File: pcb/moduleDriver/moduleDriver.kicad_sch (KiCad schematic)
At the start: 42 parts, among them J1 MOTOR, J10 Sensor, J11 Power, J12 Power, J13 Power, J14 LOOPBACK, J2 MOTOR, J3 MOTOR, J4 MOTOR, J5 IDC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

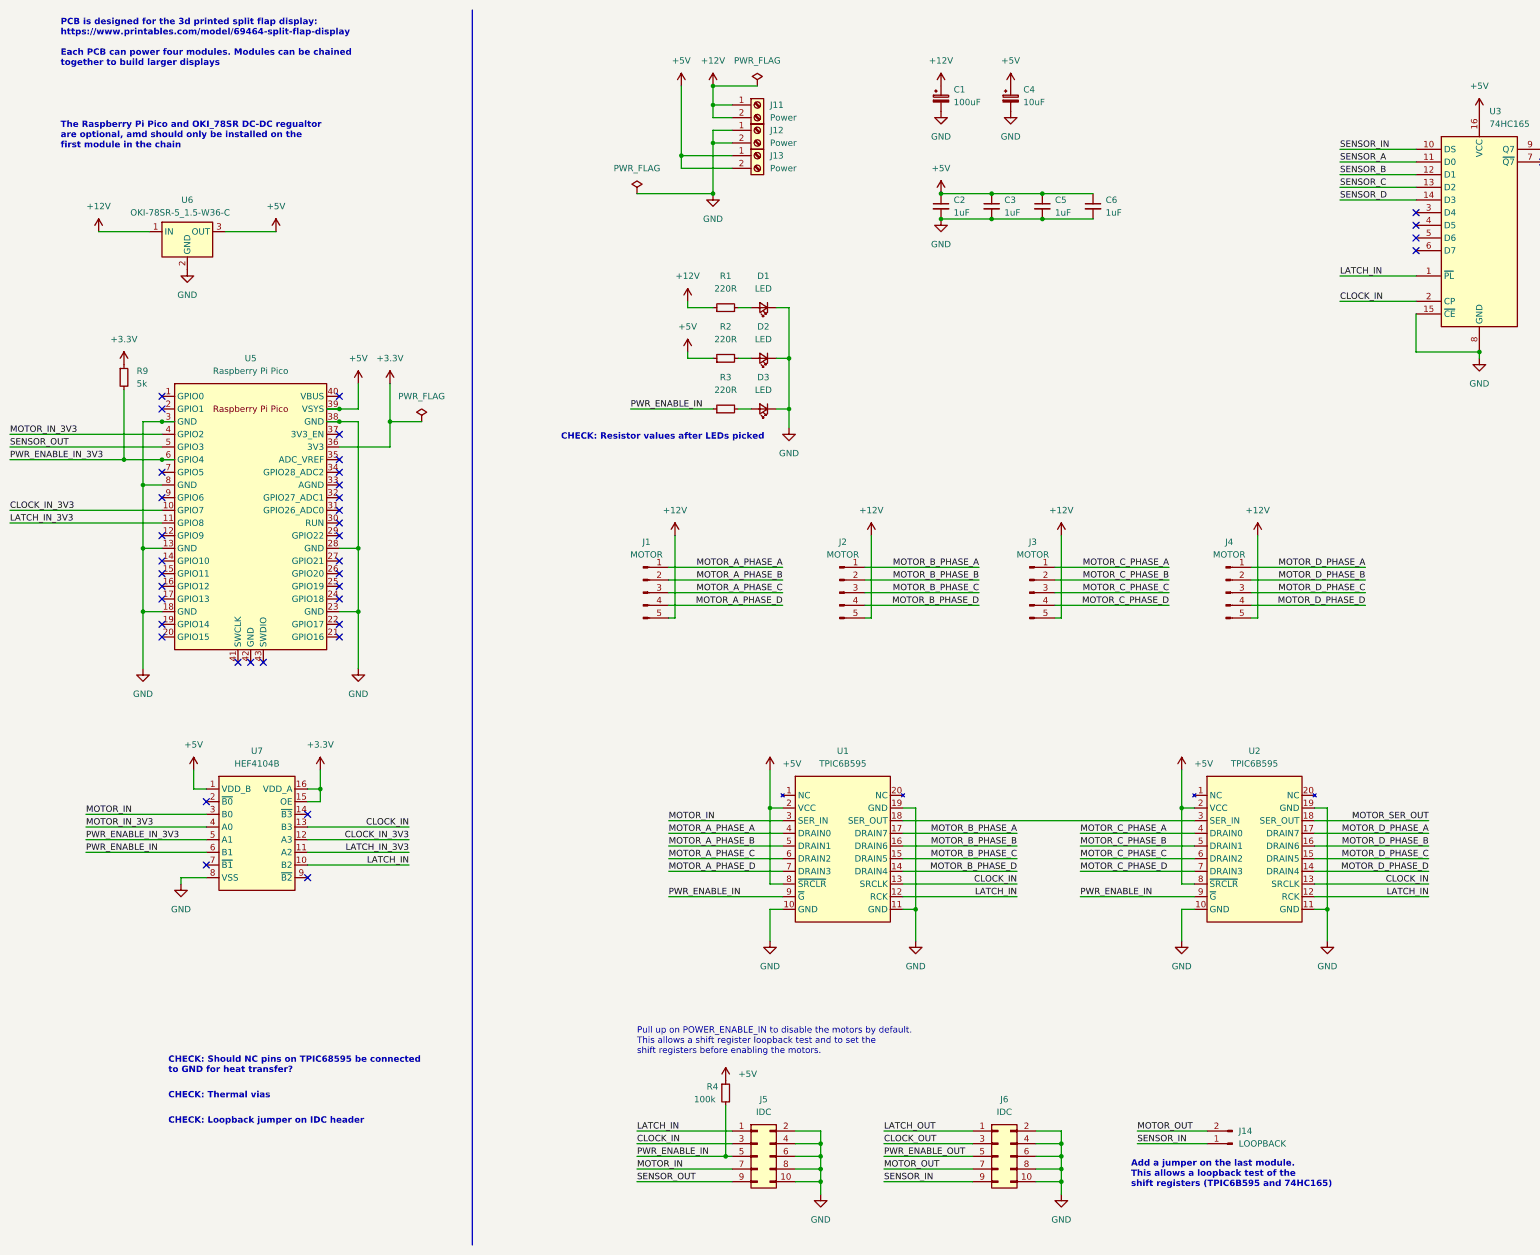
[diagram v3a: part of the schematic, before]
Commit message: Add voltage divider for SENSOR_OUT
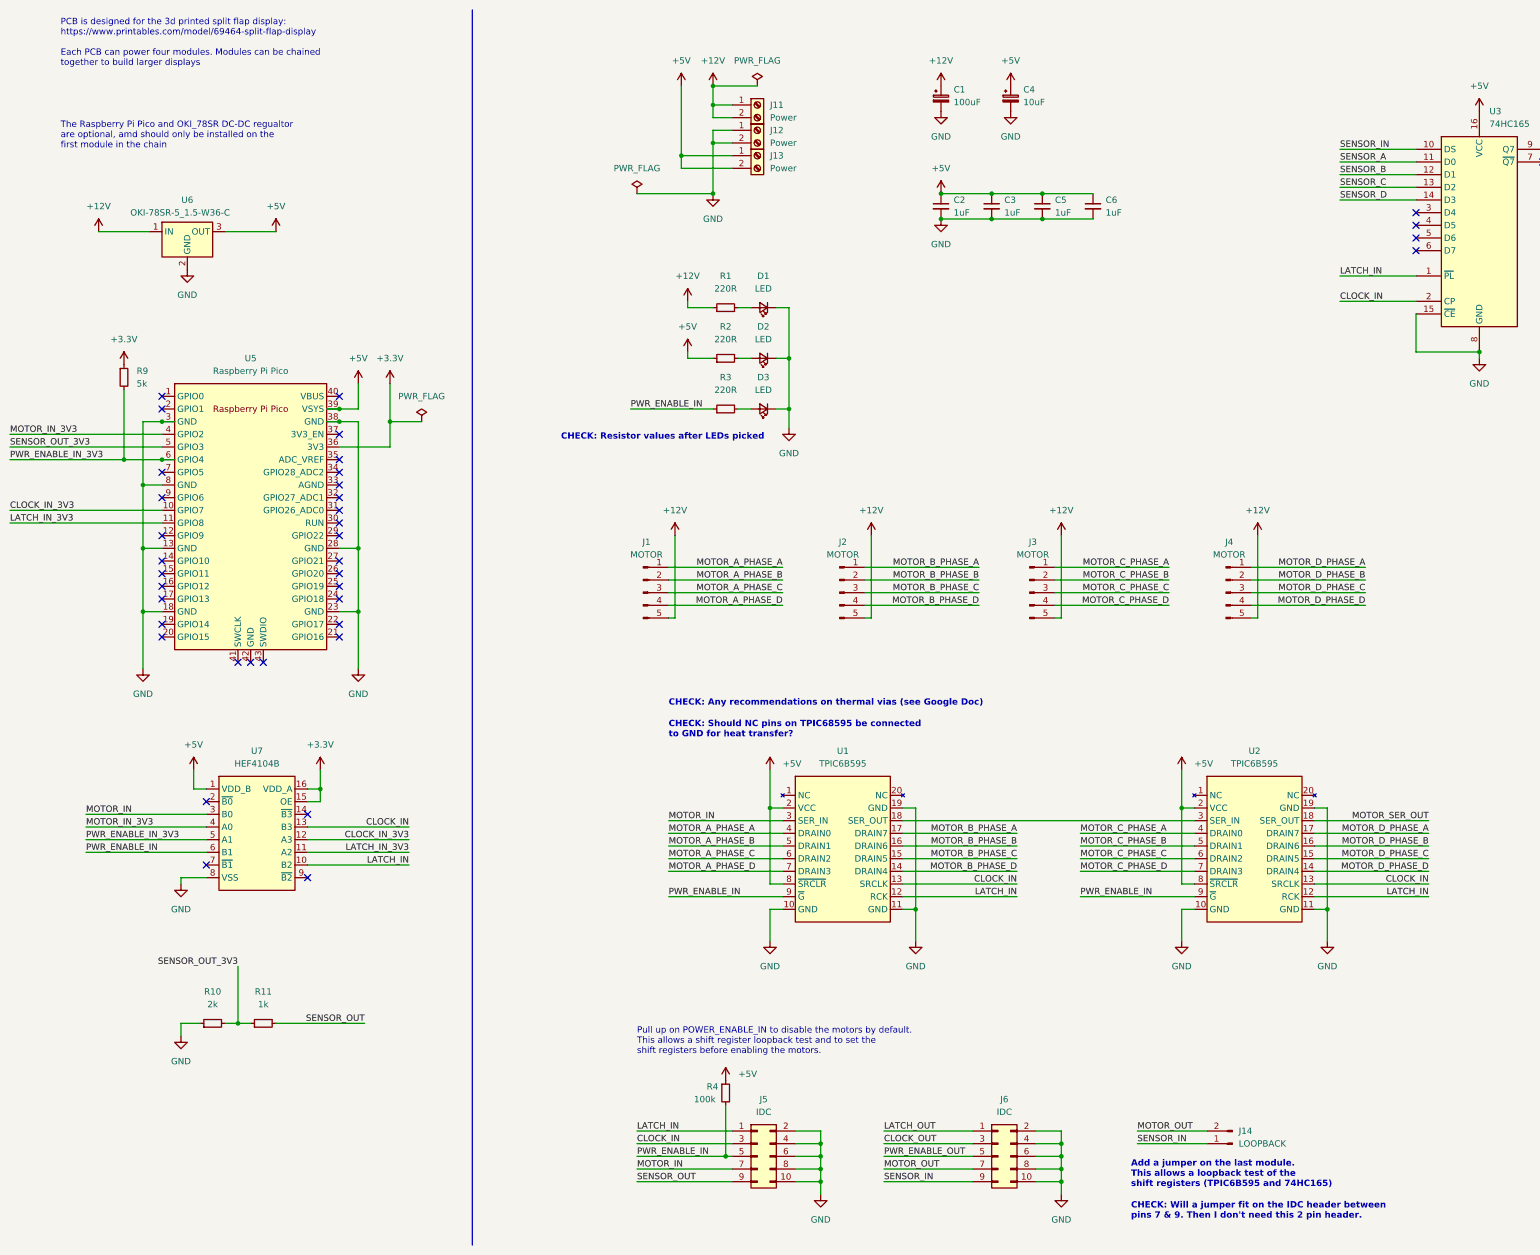
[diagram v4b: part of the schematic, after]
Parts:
- added R10: 2k, Resistor_SMD:R_0603_1608Metric, symbol Device:R_Small
- added R11: 1k, Resistor_SMD:R_0603_1608Metric, symbol Device:R_Small
- U7: footprint (none) -> Package_SO:SOIC-16_4.55x10.3mm_P1.27mm
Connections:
- net GND: now also R10.1
- net SENSOR_OUT: now also R11.2; no longer U5.5 (GPIO3)
- new net SENSOR_OUT_3V3: R10.2, R11.1, U5.5 (GPIO3)
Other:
- note added: "CHECK: Any recommendations on thermal vias (see Google Doc)"
- note added: "CHECK: Will a jumper fit on the IDC header between pins 7 & 9. Then I don't need this 2 pin header."
- note removed: "CHECK: Loopback jumper on IDC header"
- note removed: "CHECK: Thermal vias"
- title: (none) -> Split Flap Module
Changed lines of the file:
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@@
 (kicad_sch (version 20211123) (generator eeschema)
   (paper "A3")
+  (title_block
+    (title "Split Flap Module")
+    (rev "0.2")
+  )
   (junction (at 374.65 64.77) (diameter 0) (color 0 0 0 0)
   )
@@
   )
   (junction (at 41.91 143.51) (diameter 0) (color 0 0 0 0)
+  )
+  (junction (at 60.96 226.06) (diameter 0) (color 0 0 0 0)
   )
   (junction (at 38.1 113.03) (diameter 0) (color 0 0 0 0)
@@
     (stroke (width 0) (type default) (color 0 0 0 0))
   )
+  (wire (pts (xy 60.96 226.06) (xy 63.5 226.06))
+    (stroke (width 0) (type default) (color 0 0 0 0))
+  )
   (wire (pts (xy 186.69 139.7) (xy 209.55 139.7))
     (stroke (width 0) (type default) (color 0 0 0 0))
@@
     (stroke (width 0) (type default) (color 0 0 0 0))
   )
+  (wire (pts (xy 49.53 226.06) (xy 49.53 228.6))
+    (stroke (width 0) (type default) (color 0 0 0 0))
+  )
   (wire (pts (xy 297.18 83.82) (xy 297.18 91.44))
     (stroke (width 0) (type default) (color 0 0 0 0))
@@
     (stroke (width 0) (type default) (color 0 0 0 0))
   )
+  (wire (pts (xy 53.34 226.06) (xy 49.53 226.06))
+    (stroke (width 0) (type default) (color 0 0 0 0))
+  )
   (wire (pts (xy 364.49 40.64) (xy 364.49 39.37))
     (stroke (width 0) (type default) (color 0 0 0 0))
@@
     (stroke (width 0) (type default) (color 0 0 0 0))
   )
+  (wire (pts (xy 68.58 226.06) (xy 86.36 226.06))
+    (stroke (width 0) (type default) (color 0 0 0 0))
+  )
   (wire (pts (xy 147.32 139.7) (xy 170.18 139.7))
     (stroke (width 0) (type default) (color 0 0 0 0))
@@
     (stroke (width 0) (type default) (color 0 0 0 0))
   )
+  (wire (pts (xy 58.42 226.06) (xy 60.96 226.06))
+    (stroke (width 0) (type default) (color 0 0 0 0))
+  )
   (wire (pts (xy 351.79 45.72) (xy 364.49 45.72))
     (stroke (width 0) (type default) (color 0 0 0 0))
@@
     (stroke (width 0) (type default) (color 0 0 0 0))
   )
+  (wire (pts (xy 60.96 214.63) (xy 60.96 226.06))
+    (stroke (width 0) (type default) (color 0 0 0 0))
+  )
   (wire (pts (xy 151.13 91.44) (xy 151.13 92.71))
     (stroke (width 0) (type default) (color 0 0 0 0))
@@
   )
   (text "CHECK: Should NC pins on TPIC68595 be connected\nto GND for heat transfer?\n"
-    (at 46.99 236.22 0)
+    (at 147.32 168.91 0)
     (effects (font (size 1.27 1.27) (thickness 0.254) bold) (justify left bottom))
   )
@@
     (effects (font (size 1.27 1.27)) (justify left bottom))
   )
-  (text "CHECK: Loopback jumper on IDC header\n" (at 46.99 246.38 0)
+  (text "CHECK: Will a jumper fit on the IDC header between\npins 7 & 9. Then I don't need this 2 pin header.\n"
+    (at 240.03 265.43 0)
     (effects (font (size 1.27 1.27) (thickness 0.254) bold) (justify left bottom))
   )
@@
   (text "The Raspberry Pi Pico and OKI_78SR DC-DC regualtor\nare optional, amd should only be installed on the\nfirst module in the chain"
     (at 25.4 50.8 0)
-    (effects (font (size 1.27 1.27) (thickness 0.254) bold) (justify left bottom))
+    (effects (font (size 1.27 1.27)) (justify left bottom))
   )
   (text "CHECK: Resistor values after LEDs picked" (at 125.73 109.22 0)
     (effects (font (size 1.27 1.27) bold) (justify left bottom))
   )
-  (text "CHECK: Thermal vias\n" (at 46.99 241.3 0)
+  (text "CHECK: Any recommendations on thermal vias (see Google Doc)\n"
+    (at 147.32 162.56 0)
     (effects (font (size 1.27 1.27) (thickness 0.254) bold) (justify left bottom))
   )
   (text "PCB is designed for the 3d printed split flap display:\nhttps://www.printables.com/model/69464-split-flap-display\n\nEach PCB can power four modules. Modules can be chained\ntogether to build larger displays"
     (at 25.4 34.29 0)
-    (effects (font (size 1.27 1.27) (thickness 0.254) bold) (justify left bottom))
+    (effects (font (size 1.27 1.27)) (justify left bottom))
   )
   (label "PWR_ENABLE_IN" (at 328.93 185.42 0)
@@
     (effects (font (size 1.27 1.27)) (justify left bottom))
   )
+  (label "SENSOR_OUT_3V3" (at 60.96 214.63 180)
+    (effects (font (size 1.27 1.27)) (justify right bottom))
+  )
   (label "MOTOR_C_PHASE_C" (at 247.65 139.7 180)
     (effects (font (size 1.27 1.27)) (justify right bottom))
@@
     (effects (font (size 1.27 1.27)) (justify right bottom))
   )
+  (label "SENSOR_OUT" (at 86.36 226.06 180)
+    (effects (font (size 1.27 1.27)) (justify right bottom))
+  )
   (label "MOTOR_D_PHASE_B" (at 299.72 190.5 180)
     (effects (font (size 1.27 1.27)) (justify right bottom))
@@
     (effects (font (size 1.27 1.27)) (justify left bottom))
   )
-  (label "SENSOR_OUT" (at 15.24 110.49 0)
+  (label "SENSOR_OUT_3V3" (at 15.24 110.49 0)
     (effects (font (size 1.27 1.27)) (justify left bottom))
   )
@@
     (pin "2")
   )
+  (symbol (lib_id "Device:R_Small") (at 55.88 226.06 90) (unit 1)
+    (in_bom yes) (on_board yes) (fields_autoplaced)
+    (property "Reference" "R10" (id 0) (at 55.88 219.71 90))
+    (property "Value" "2k" (id 1) (at 55.88 222.25 90))
+    (property "Footprint" "Resistor_SMD:R_0603_1608Metric" (id 2) (at 55.88 226.06 0)
+      (effects (font (size 1.27 1.27)) hide)
+    )
+    (property "Datasheet" "~" (id 3) (at 55.88 226.06 0)
+      (effects (font (size 1.27 1.27)) hide)
+    )
+    (pin "1")
+    (pin "2")
+  )
   (symbol (lib_id "Connector:Screw_Terminal_01x02") (at 165.1 46.99 0) (unit 1)
     (in_bom yes) (on_board yes) (fields_autoplaced)
@@
     )
     (property "Datasheet" "" (id 3) (at 41.91 154.94 0)
+      (effects (font (size 1.27 1.27)) hide)
+    )
+    (pin "1")
+  )
+  (symbol (lib_id "power:GND") (at 49.53 228.6 0) (unit 1)
+    (in_bom yes) (on_board yes) (fields_autoplaced)
+    (property "Reference" "#PWR012" (id 0) (at 49.53 234.95 0)
+      (effects (font (size 1.27 1.27)) hide)
+    )
+    (property "Value" "GND" (id 1) (at 49.53 233.68 0))
+    (property "Footprint" "" (id 2) (at 49.53 228.6 0)
+      (effects (font (size 1.27 1.27)) hide)
+    )
+    (property "Datasheet" "" (id 3) (at 49.53 228.6 0)
       (effects (font (size 1.27 1.27)) hide)
     )
@@
     (property "Reference" "U7" (id 0) (at 64.77 171.45 0))
     (property "Value" "HEF4104B" (id 1) (at 64.77 173.99 0))
-    (property "Footprint" "" (id 2) (at 63.5 179.07 0)
+    (property "Footprint" "Package_SO:SOIC-16_4.55x10.3mm_P1.27mm" (id 2) (at 63.5 179.07 0)
       (effects (font (size 1.27 1.27)) hide)
     )
@@
     )
     (property "Datasheet" "~" (id 3) (at 222.25 62.23 0)
+      (effects (font (size 1.27 1.27)) hide)
+    )
+    (pin "1")
+    (pin "2")
+  )
+  (symbol (lib_id "Device:R_Small") (at 66.04 226.06 90) (unit 1)
+    (in_bom yes) (on_board yes) (fields_autoplaced)
+    (property "Reference" "R11" (id 0) (at 66.04 219.71 90))
+    (property "Value" "1k" (id 1) (at 66.04 222.25 90))
+    (property "Footprint" "Resistor_SMD:R_0603_1608Metric" (id 2) (at 66.04 226.06 0)
+      (effects (font (size 1.27 1.27)) hide)
+    )
+    (property "Datasheet" "~" (id 3) (at 66.04 226.06 0)
       (effects (font (size 1.27 1.27)) hide)
     )
@@
       (reference "#PWR011") (unit 1) (value "GND") (footprint "")
     )
+    (path "/b7679883-c4d6-479b-b2e8-8d429a361f77"
+      (reference "#PWR012") (unit 1) (value "GND") (footprint "")
+    )
     (path "/e98e8bd9-6e5c-4a53-a111-31034a67ec35"
       (reference "#PWR013") (unit 1) (value "GND") (footprint "")
@@
       (reference "R9") (unit 1) (value "5k") (footprint "Resistor_SMD:R_0603_1608Metric")
     )
+    (path "/3e3ecd2d-0bfb-4e50-bcc0-1bef6ba0007a"
+      (reference "R10") (unit 1) (value "2k") (footprint "Resistor_SMD:R_0603_1608Metric")
+    )
+    (path "/f7cad68f-8ced-4c99-ba1e-3e8c37501d6b"
+      (reference "R11") (unit 1) (value "1k") (footprint "Resistor_SMD:R_0603_1608Metric")
+    )
     (path "/baba20a9-3d04-4395-8e99-155a6692ce1b"
       (reference "U1") (unit 1) (value "TPIC6B595") (footprint "Package_SO:SOIC-20W_7.5x12.8mm_P1.27mm")
@@
     )
     (path "/cc31eac7-bfa1-4f9a-8f21-bb8b7d3762d0"
-      (reference "U7") (unit 1) (value "HEF4104B") (footprint "")
-    )
-  )
+      (reference "U7") (unit 1) (value "HEF4104B") (footprint "Package_SO:SOIC-16_4.55x10.3mm_P1.27mm")
+    )
+  )
